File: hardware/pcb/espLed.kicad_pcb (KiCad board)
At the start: 2 copper layers, 23 parts, among them J1 led_strip, J2 flashing, J3 power, Q1 IRF9310TRPBF, Q2 AO3400A, Q3 AO3400A, Q4 AO3400A, SW1 reset, SW2 flash, U1 AMS1117-3.3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

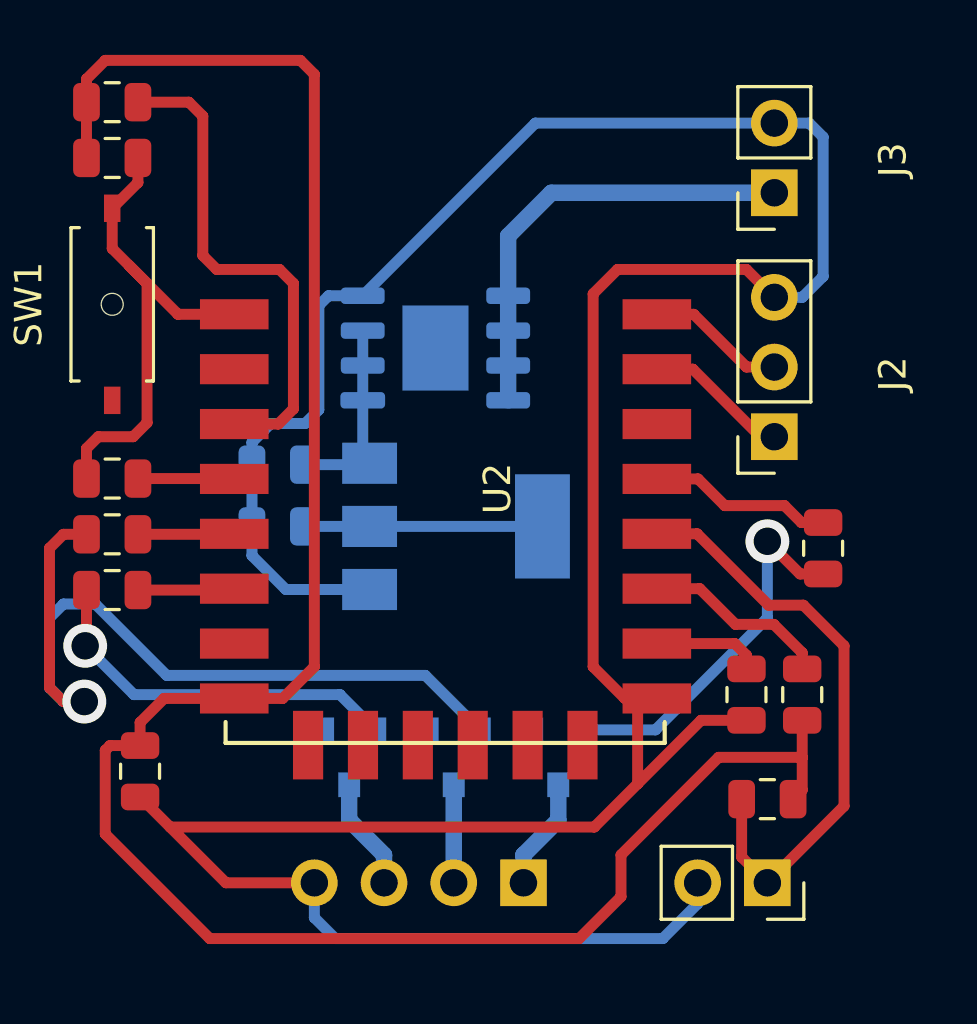
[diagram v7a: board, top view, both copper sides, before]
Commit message: replace GND with 12V in led strip connector
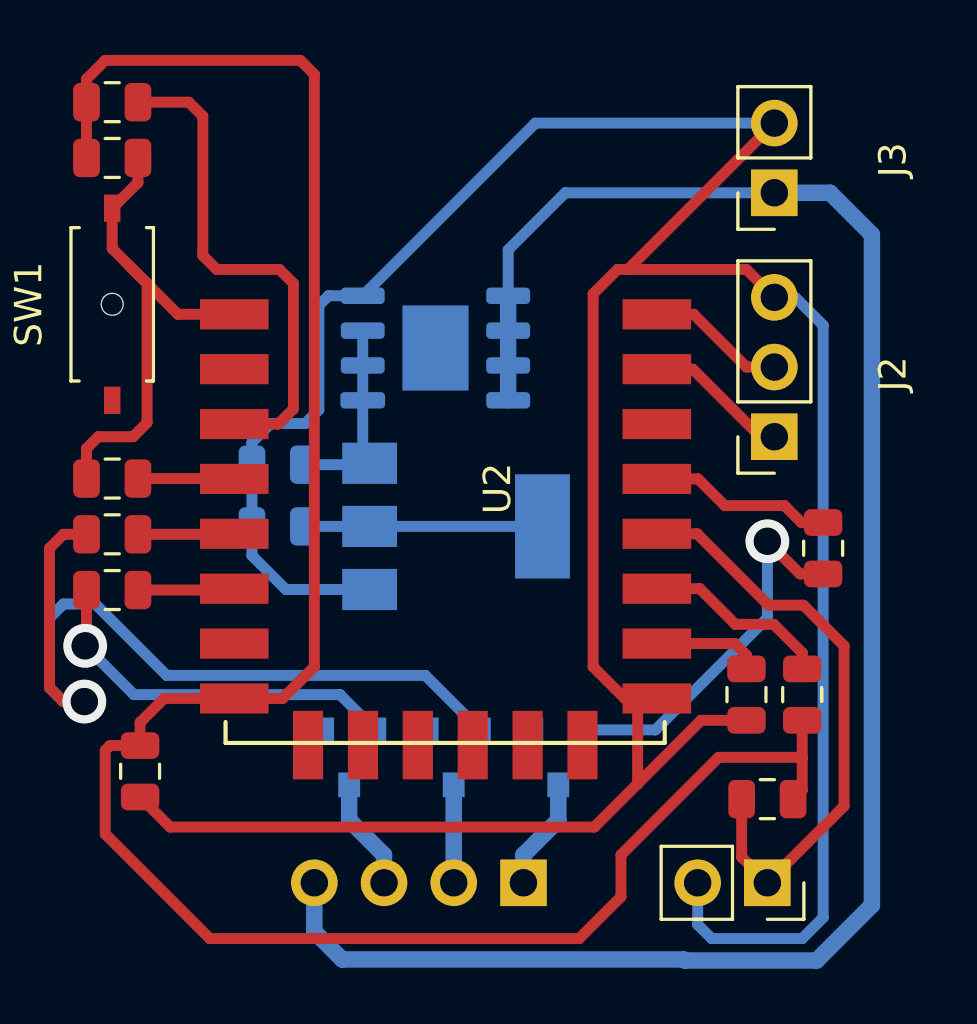
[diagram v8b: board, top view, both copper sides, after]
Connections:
- J1 pad 4: GND -> /12v_in
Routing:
- net /12v_in: track 16.3 -> 68.0 mm
- net GND: track 117.5 -> 124.1 mm
